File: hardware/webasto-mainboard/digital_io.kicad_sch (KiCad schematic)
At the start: 46 parts

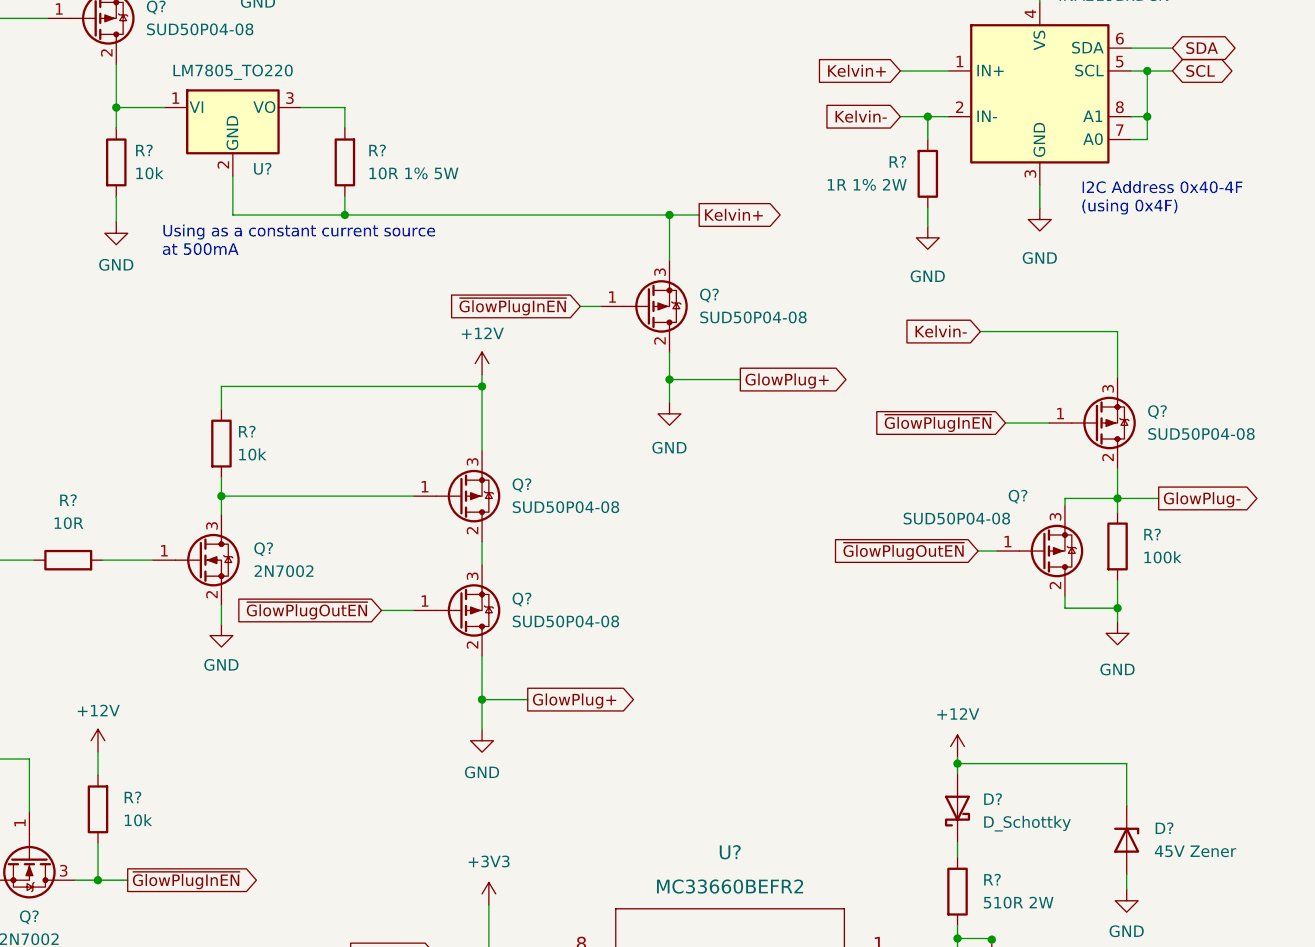
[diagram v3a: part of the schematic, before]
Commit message: Added all the other sensor implementations
- using classes in C++ is nice :)
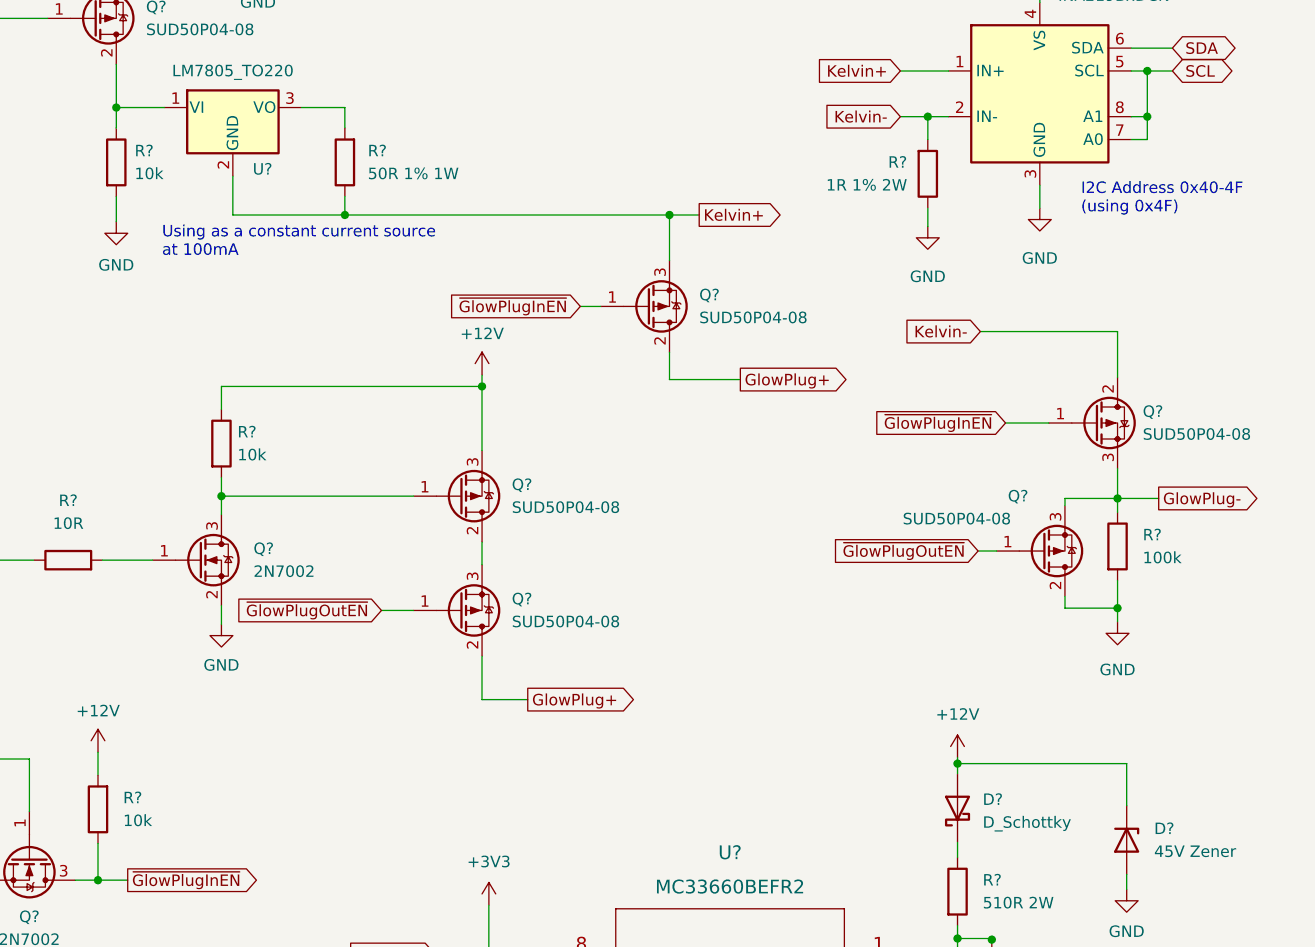
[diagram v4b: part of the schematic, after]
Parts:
- R?: value 10R 1% 5W -> 50R 1% 1W; footprint UltraLibrarian:355010RFT -> Resistor_SMD:R_2816_7142Metric_Pad3.20x4.45mm_HandSolder
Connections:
- net GND: no longer Q?.2 (D), Q?.2 (D)
- net GlowPlug-: now also Q?.3 (S); no longer Q?.2 (D)
- net Kelvin-: now also Q?.2 (D); no longer Q?.3 (S)
- new net GlowPlug+: Q?.2 (D), Q?.2 (D)
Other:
- note added: "Using as a constant current source at 100mA"
- note removed: "Using as a constant current source at 500mA"
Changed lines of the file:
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@@
   (junction (at 151.384 37.084) (diameter 0) (color 0 0 0 0)
   )
-  (junction (at 192.024 102.87) (diameter 0) (color 0 0 0 0)
-  )
   (junction (at 241.554 38.1) (diameter 0) (color 0 0 0 0)
   )
@@
   (junction (at 149.352 156.718) (diameter 0) (color 0 0 0 0)
   )
-  (junction (at 212.852 67.31) (diameter 0) (color 0 0 0 0)
-  )
   (junction (at 265.938 33.02) (diameter 0) (color 0 0 0 0)
   )
@@
     (stroke (width 0) (type default) (color 0 0 0 0))
   )
-  (wire (pts (xy 212.852 67.31) (xy 212.852 69.85))
-    (stroke (width 0) (type default) (color 0 0 0 0))
-  )
   (wire (pts (xy 41.656 85.598) (xy 46.736 85.598))
     (stroke (width 0) (type default) (color 0 0 0 0))
@@
   )
   (wire (pts (xy 68.072 121.158) (xy 76.2 121.158))
-    (stroke (width 0) (type default) (color 0 0 0 0))
-  )
-  (wire (pts (xy 192.024 102.87) (xy 192.024 106.172))
     (stroke (width 0) (type default) (color 0 0 0 0))
   )
@@
     (effects (font (size 1.27 1.27)) (justify left bottom))
   )
-  (text "Using as a constant current source\nat 500mA" (at 156.464 53.848 0)
+  (text "Using as a constant current source\nat 100mA" (at 156.464 53.848 0)
     (effects (font (size 1.27 1.27)) (justify left bottom))
   )
@@
   )
   (symbol (lib_id "Device:R") (at 176.784 43.18 180) (unit 1)
-    (in_bom yes) (on_board yes) (fields_autoplaced)
+    (in_bom yes) (on_board yes)
     (property "Reference" "R?" (id 0) (at 179.324 41.9099 0)
       (effects (font (size 1.27 1.27)) (justify right))
     )
-    (property "Value" "10R 1% 5W" (id 1) (at 179.324 44.4499 0)
+    (property "Value" "50R 1% 1W" (id 1) (at 179.324 44.4499 0)
       (effects (font (size 1.27 1.27)) (justify right))
     )
-    (property "Footprint" "UltraLibrarian:355010RFT" (id 2) (at 178.562 43.18 90)
+    (property "Footprint" "Resistor_SMD:R_2816_7142Metric_Pad3.20x4.45mm_HandSolder" (id 2) (at 178.562 43.18 90)
       (effects (font (size 1.27 1.27)) hide)
     )
@@
     (pin "3")
   )
-  (symbol (lib_name "GND_1") (lib_id "power:GND") (at 192.024 106.172 0) (unit 1)
-    (in_bom yes) (on_board yes) (fields_autoplaced)
-    (property "Reference" "#PWR?" (id 0) (at 192.024 112.522 0)
-      (effects (font (size 1.27 1.27)) hide)
-    )
-    (property "Value" "GND" (id 1) (at 192.024 110.998 0))
-    (property "Footprint" "" (id 2) (at 192.024 106.172 0)
-      (effects (font (size 1.27 1.27)) hide)
-    )
-    (property "Datasheet" "" (id 3) (at 192.024 106.172 0)
-      (effects (font (size 1.27 1.27)) hide)
-    )
-    (pin "1")
-  )
   (symbol (lib_name "GND_1") (lib_id "power:GND") (at 83.312 89.916 0) (unit 1)
     (in_bom yes) (on_board yes) (fields_autoplaced)
@@
     (pin "3")
   )
-  (symbol (lib_id "Transistor_FET:SUD50P04-08") (at 260.096 72.136 0) (mirror x) (unit 1)
-    (in_bom yes) (on_board yes) (fields_autoplaced)
-    (property "Reference" "Q?" (id 0) (at 265.938 70.8659 0)
-      (effects (font (size 1.27 1.27)) (justify left))
-    )
-    (property "Value" "SUD50P04-08" (id 1) (at 265.938 73.4059 0)
-      (effects (font (size 1.27 1.27)) (justify left))
-    )
-    (property "Footprint" "Package_TO_SOT_SMD:TO-252-2" (id 2) (at 265.049 70.231 0)
+  (symbol (lib_id "Transistor_FET:SUD50P04-08") (at 260.096 72.136 0) (unit 1)
+    (in_bom yes) (on_board yes) (fields_autoplaced)
+    (property "Reference" "Q?" (id 0) (at 265.43 70.8659 0)
+      (effects (font (size 1.27 1.27)) (justify left))
+    )
+    (property "Value" "SUD50P04-08" (id 1) (at 265.43 73.4059 0)
+      (effects (font (size 1.27 1.27)) (justify left))
+    )
+    (property "Footprint" "Package_TO_SOT_SMD:TO-252-2" (id 2) (at 265.049 74.041 0)
       (effects (font (size 1.27 1.27) italic) (justify left) hide)
     )
@@
     (pin "2")
   )
-  (symbol (lib_name "GND_6") (lib_id "power:GND") (at 212.852 69.85 0) (unit 1)
-    (in_bom yes) (on_board yes) (fields_autoplaced)
-    (property "Reference" "#PWR?" (id 0) (at 212.852 76.2 0)
-      (effects (font (size 1.27 1.27)) hide)
-    )
-    (property "Value" "GND" (id 1) (at 212.852 74.93 0))
-    (property "Footprint" "" (id 2) (at 212.852 69.85 0)
-      (effects (font (size 1.27 1.27)) hide)
-    )
-    (property "Datasheet" "" (id 3) (at 212.852 69.85 0)
-      (effects (font (size 1.27 1.27)) hide)
-    )
-    (pin "1")
-  )
   (symbol (lib_name "+12V_3") (lib_id "power:+12V") (at 149.352 142.494 0) (unit 1)

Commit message: v1.0 layout complete
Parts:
- removed Q?: SUD50P04-08, Package_TO_SOT_SMD:TO-252-2, symbol Transistor_FET:SUD50P04-08
- added C4: 100nF 25V, Capacitor_SMD:C_0603_1608Metric_Pad1.08x0.95mm_HandSolder, symbol Device:C
- added D1: ACDBQC0130L-HF, Diode_SMD:D_SOD-923, symbol Device:D_Schottky
- added Q12: SSM3J374R, Package_TO_SOT_SMD:SOT-23, symbol Transistor_FET:AO3401A
- added R10, R11, R12, R9: 10R, Resistor_SMD:R_0805_2012Metric_Pad1.20x1.40mm_HandSolder, symbol Device:R
- added R13: 10k, Resistor_SMD:R_0805_2012Metric_Pad1.20x1.40mm_HandSolder, symbol Device:R
- C3: renamed from C?; value 220nF -> 100nF 25V; footprint (none) -> Capacitor_SMD:C_0805_2012Metric_Pad1.18x1.45mm_HandSolder
- C5, C6, C7: renamed from C?; footprint (none) -> Capacitor_SMD:C_0805_2012Metric
- D2: renamed from D?; value D_Schottky -> ACDBQC0130L-HF; footprint (none) -> Diode_SMD:D_SOD-923
- D3: renamed from D?; value 27V Zener -> BZT52C27-7-F; footprint (none) -> Diode_SMD:D_SOD-123
- D4: renamed from D?; value 45V Zener -> MMSZ5260C-E3-08; footprint (none) -> Diode_SMD:D_SOD-123
- R1, R14, R15, R16, R17, R18, R19, R2, R20, R24, R3, R4, R5, R6, R7, R8: renamed from R?; footprint (none) -> Resistor_SMD:R_0805_2012Metric_Pad1.20x1.40mm_HandSolder
- R22, R23: renamed from R?; footprint (none) -> Resistor_SMD:R_2512_6332Metric_Pad1.40x3.35mm_HandSolder
- U4: renamed from U?; footprint SO8_SOT96-4_NXP -> UltraLibrarian:MC33660BEFR2
- gave numbers to parts that had none: 19
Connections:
- net +12V: now also C3.2, C4.2, Q12.2 (S); no longer C3.1
- net +3V3: now also R13.1
- net GND: now also C3.1, C4.1, R10.2, R11.2, R12.2, R9.2; no longer C3.2, Q6.2 (D), Q7.2 (D), Q8.2 (D), Q9.2 (D)
- net ~{GlowPlugInEN}: now also Q12.1 (G)
- net at R19.1, U3.1 (VI): now also Q12.3 (D)
- new net CirculationPump: Q7.2 (D), R10.1
- new net CombustionFan: Q6.2 (D), R9.1
- new net FuelPump: Q8.2 (D), R11.1
- new net StartRun: D1.1 (K)
- new net StartRun3V: D1.2 (A), R13.2
- new net VehicleFanRelay: Q9.2 (D), R12.1
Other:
- note added: "27V Zener 500mw"
- note added: "43V Zener 500mW"
- moved on the sheet: C3

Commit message: Added title block info
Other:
- title: (none) -> Webasto Thermo Top C Replacement Controller
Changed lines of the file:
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@@
 (kicad_sch (version 20211123) (generator eeschema)
   (paper "A4")
+  (title_block
+    (title "Webasto Thermo Top C Replacement Controller")
+    (date "2023-01-19")
+    (rev "v1.0")
+  )
   (junction (at 68.072 121.158) (diameter 0) (color 0 0 0 0)
   )

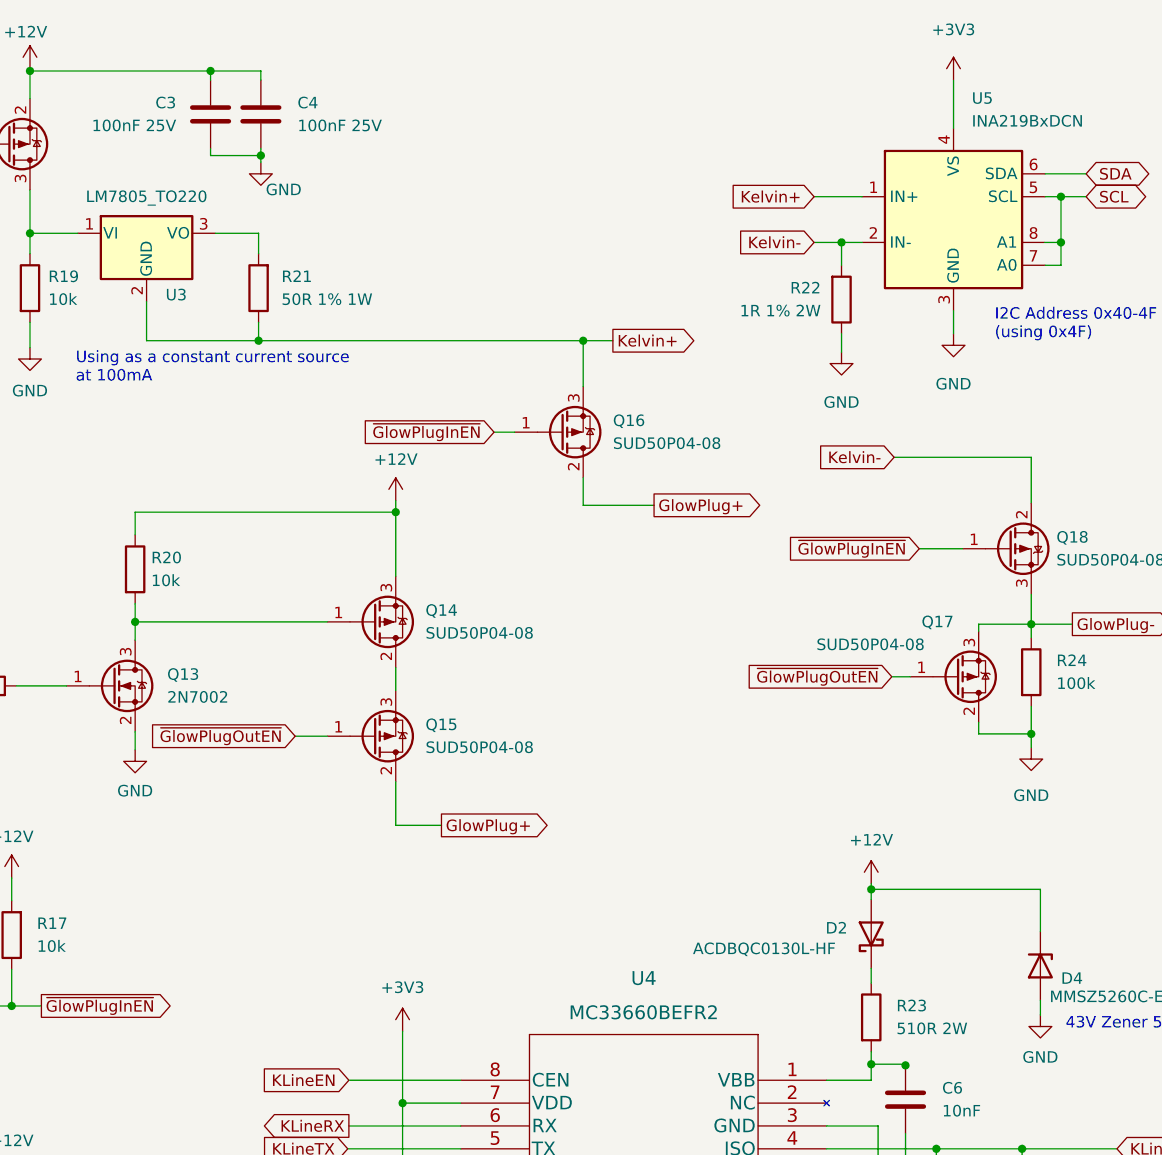
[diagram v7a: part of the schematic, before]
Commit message: Added a 4kbit FRAM on the mainboard to hold nonvolatile
- things like burn hours.
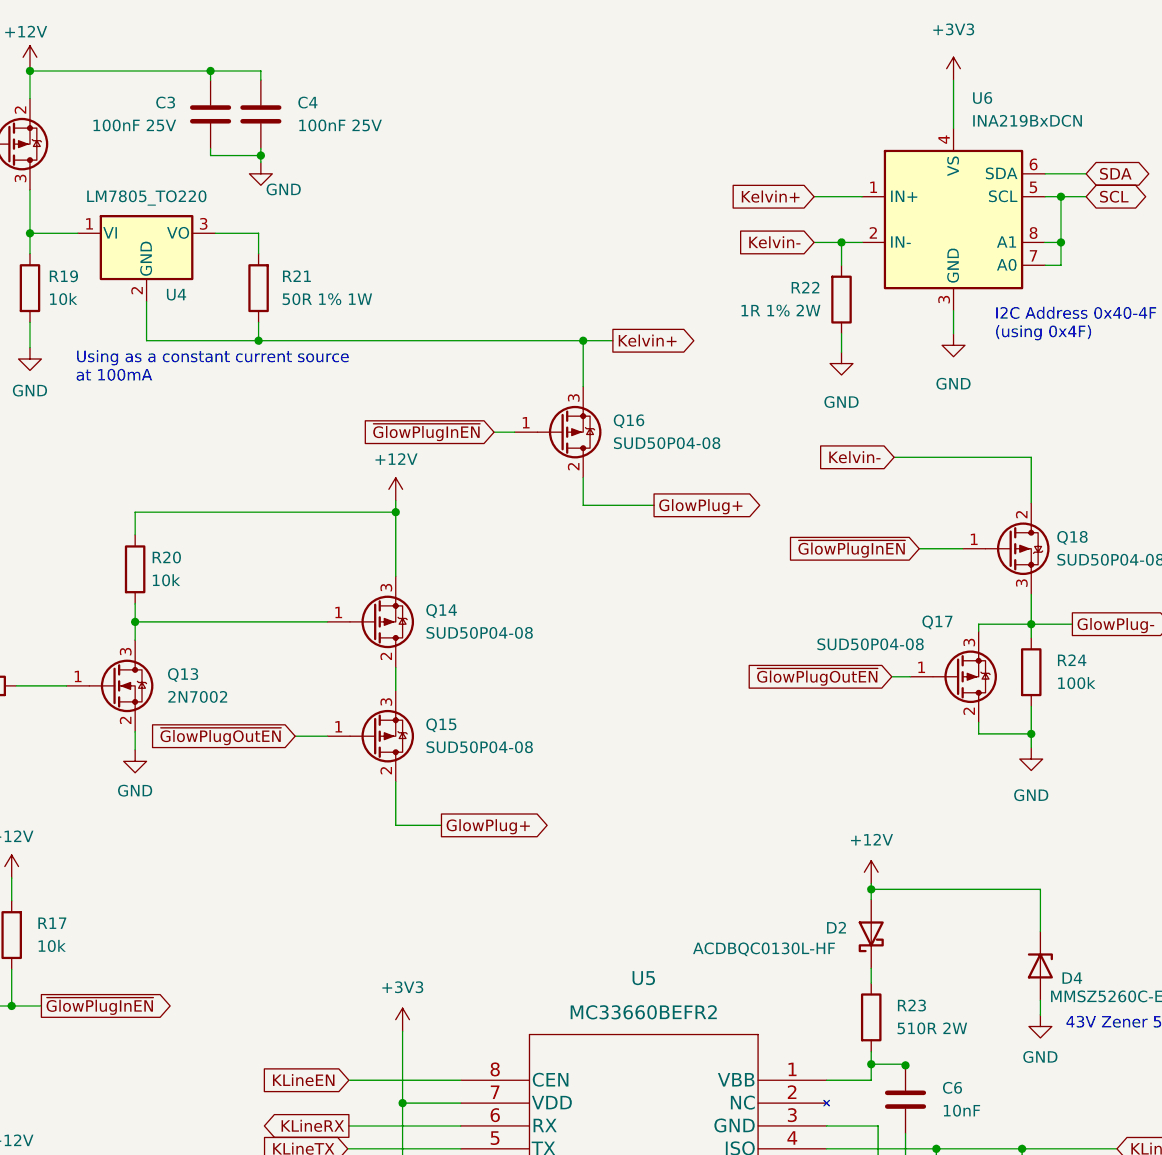
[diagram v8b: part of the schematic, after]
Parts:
- renumbered U3 to U4, U4 to U5, U5 to U6
